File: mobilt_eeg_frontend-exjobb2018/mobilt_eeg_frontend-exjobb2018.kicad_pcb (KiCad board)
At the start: 2 copper layers, 91 x 90.4 mm, 125 parts, among them J1 Conn_02x04_Odd_Even, J11 Conn_01x02, J2 Conn_02x20_Odd_Even, J3 Conn_02x04_Odd_Even, J5 Data Header, J8 Conn_01x08, J9 Conn_01x04, P1 Conn_02x20_Odd_Even, SW1 SW_DIP_x01, SW2 SW_DIP_x01, U1 ADS1299-4PAG, U2 TPS60403DBVR, U3 TPS72325DBVT, U4 TPS73225DBVT, U5 TPS73233DBVT, U6 CAT24C256, X1 X1G0044810050_SG7050CAN_2.048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

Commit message: eagle import experiments
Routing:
- net AVDD: track 76.9 -> 69.5 mm
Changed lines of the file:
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@@
     (thickness 1.6)
     (drawings 156)
-    (tracks 990)
+    (tracks 985)
     (zones 0)
     (modules 125)
@@
     (pad_to_mask_clearance 0)
     (aux_axis_origin 200 150)
-    (grid_origin 208.37 96.23)
     (visible_elements 7FFFFFFF)
     (pcbplotparams
@@
     (add_net GNDD)
   )
+  (module LEDs:LED_D3.0mm (layer F.Cu)
+    (at 259.5 124.5)
+    (descr "LED, diameter 3.0mm, 2 pins")
+    (tags "LED diameter 3.0mm 2 pins")
+    (fp_text reference D1 (at 4.5 0 90) (layer F.SilkS)
+      (effects (font (size 1 1) (thickness 0.15)))
+    )
+    (fp_text value LED (at 1.27 2.96) (layer F.Fab)
+      (effects (font (size 1 1) (thickness 0.15)))
+    )
+    (fp_line (start 3.7 -2.25) (end -1.15 -2.25) (layer F.CrtYd) (width 0.05))
+    (fp_line (start 3.7 2.25) (end 3.7 -2.25) (layer F.CrtYd) (width 0.05))
+    (fp_line (start -1.15 2.25) (end 3.7 2.25) (layer F.CrtYd) (width 0.05))
+    (fp_line (start -1.15 -2.25) (end -1.15 2.25) (layer F.CrtYd) (width 0.05))
+    (fp_line (start -0.29 1.08) (end -0.29 1.236) (layer F.SilkS) (width 0.12))
+    (fp_line (start -0.29 -1.236) (end -0.29 -1.08) (layer F.SilkS) (width 0.12))
+    (fp_line (start -0.23 -1.16619) (end -0.23 1.16619) (layer F.Fab) (width 0.1))
+    (fp_circle (center 1.27 0) (end 2.77 0) (layer F.Fab) (width 0.1))
+    (fp_arc (start 1.27 0) (end 0.229039 1.08) (angle -87.9) (layer F.SilkS) (width 0.12))
+    (fp_arc (start 1.27 0) (end 0.229039 -1.08) (angle 87.9) (layer F.SilkS) (width 0.12))
+    (fp_arc (start 1.27 0) (end -0.29 1.235516) (angle -108.8) (layer F.SilkS) (width 0.12))
+    (fp_arc (start 1.27 0) (end -0.29 -1.235516) (angle 108.8) (layer F.SilkS) (width 0.12))
+    (fp_arc (start 1.27 0) (end -0.23 -1.16619) (angle 284.3) (layer F.Fab) (width 0.1))
+    (pad 2 thru_hole circle (at 2.54 0) (size 1.8 1.8) (drill 0.9) (layers *.Cu *.Mask)
+      (net 78 "Net-(D1-Pad2)"))
+    (pad 1 thru_hole rect (at 0 0) (size 1.8 1.8) (drill 0.9) (layers *.Cu *.Mask)
+      (net 43 AGND))
+    (model ${KISYS3DMOD}/LEDs.3dshapes/LED_D3.0mm.wrl
+      (at (xyz 0 0 0))
+      (scale (xyz 0.393701 0.393701 0.393701))
+      (rotate (xyz 0 0 0))
+    )
+  )
   (module prj_lib_fp:CP_Tantalum_Case-D_EIA-7343-31_Hand (layer F.Cu)
     (at 249.885 125.61)
@@
   )
   (module LEDs:LED_D3.0mm (layer F.Cu)
-    (at 259.5 124.5)
-    (descr "LED, diameter 3.0mm, 2 pins")
-    (tags "LED diameter 3.0mm 2 pins")
-    (fp_text reference D1 (at 4.5 0 90) (layer F.SilkS)
-      (effects (font (size 1 1) (thickness 0.15)))
-    )
-    (fp_text value LED (at 1.27 2.96) (layer F.Fab)
-      (effects (font (size 1 1) (thickness 0.15)))
-    )
-    (fp_line (start 3.7 -2.25) (end -1.15 -2.25) (layer F.CrtYd) (width 0.05))
-    (fp_line (start 3.7 2.25) (end 3.7 -2.25) (layer F.CrtYd) (width 0.05))
-    (fp_line (start -1.15 2.25) (end 3.7 2.25) (layer F.CrtYd) (width 0.05))
-    (fp_line (start -1.15 -2.25) (end -1.15 2.25) (layer F.CrtYd) (width 0.05))
-    (fp_line (start -0.29 1.08) (end -0.29 1.236) (layer F.SilkS) (width 0.12))
-    (fp_line (start -0.29 -1.236) (end -0.29 -1.08) (layer F.SilkS) (width 0.12))
-    (fp_line (start -0.23 -1.16619) (end -0.23 1.16619) (layer F.Fab) (width 0.1))
-    (fp_circle (center 1.27 0) (end 2.77 0) (layer F.Fab) (width 0.1))
-    (fp_arc (start 1.27 0) (end 0.229039 1.08) (angle -87.9) (layer F.SilkS) (width 0.12))
-    (fp_arc (start 1.27 0) (end 0.229039 -1.08) (angle 87.9) (layer F.SilkS) (width 0.12))
-    (fp_arc (start 1.27 0) (end -0.29 1.235516) (angle -108.8) (layer F.SilkS) (width 0.12))
-    (fp_arc (start 1.27 0) (end -0.29 -1.235516) (angle 108.8) (layer F.SilkS) (width 0.12))
-    (fp_arc (start 1.27 0) (end -0.23 -1.16619) (angle 284.3) (layer F.Fab) (width 0.1))
-    (pad 2 thru_hole circle (at 2.54 0) (size 1.8 1.8) (drill 0.9) (layers *.Cu *.Mask)
-      (net 78 "Net-(D1-Pad2)"))
-    (pad 1 thru_hole rect (at 0 0) (size 1.8 1.8) (drill 0.9) (layers *.Cu *.Mask)
-      (net 43 AGND))
-    (model ${KISYS3DMOD}/LEDs.3dshapes/LED_D3.0mm.wrl
-      (at (xyz 0 0 0))
-      (scale (xyz 0.393701 0.393701 0.393701))
-      (rotate (xyz 0 0 0))
-    )
-  )
-  (module LEDs:LED_D3.0mm (layer F.Cu)
     (at 259.5 115.5)
     (descr "LED, diameter 3.0mm, 2 pins")
@@
     (effects (font (size 1 1) (thickness 0.15)))
   )
-  (gr_text CAMERA (at 248 138.5 90) (layer F.SilkS)
+  (gr_text CAMERA (at 247.613 138.5 90) (layer F.SilkS)
     (effects (font (size 1 1) (thickness 0.2)))
   )
@@
   (segment (start 236.36 132.8) (end 230.45 132.8) (width 0.25) (layer F.Cu) (net 70) (status 30))
   (segment (start 230.25 130) (end 230.25 133) (width 0.25) (layer F.Cu) (net 70) (status 30))
-  (segment (start 186.9692 129.7954) (end 188 128.7646) (width 0.25) (layer F.Cu) (net 70))
-  (segment (start 186.4398 129.7954) (end 186.9692 129.7954) (width 0.25) (layer F.Cu) (net 70) (status 10))
-  (segment (start 189.75 124.875) (end 189.75 124) (width 0.25) (layer F.Cu) (net 70) (status 20))
-  (segment (start 188 126.625) (end 189.75 124.875) (width 0.25) (layer F.Cu) (net 70))
-  (segment (start 188 128.7646) (end 188 126.625) (width 0.25) (layer F.Cu) (net 70))
   (segment (start 230.25 136) (end 230.25 135.125) (width 0.25) (layer F.Cu) (net 70) (status 10))
   (segment (start 238.9 135.34) (end 238.9 134.137919) (width 0.25) (layer F.Cu) (net 70) (status 10))

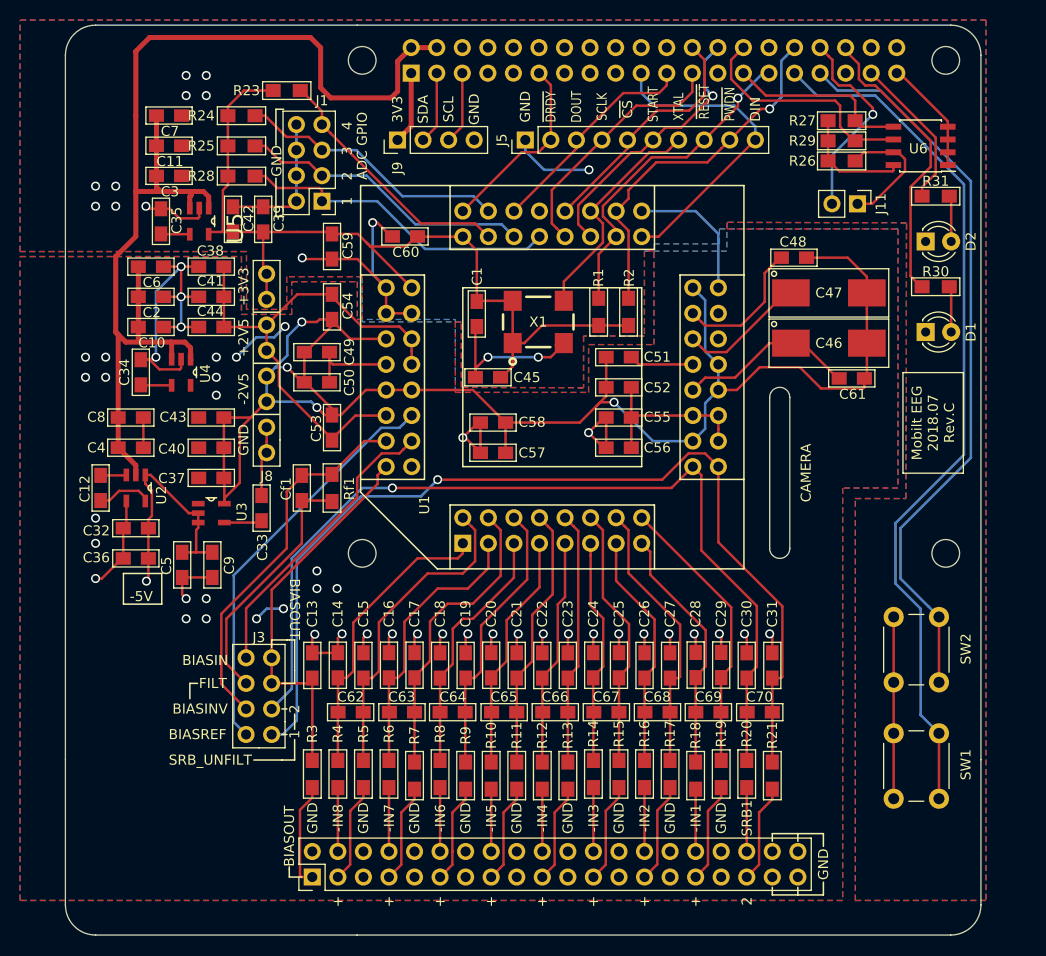
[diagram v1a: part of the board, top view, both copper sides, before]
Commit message: adjusted bias header to conform to 2.54 grid
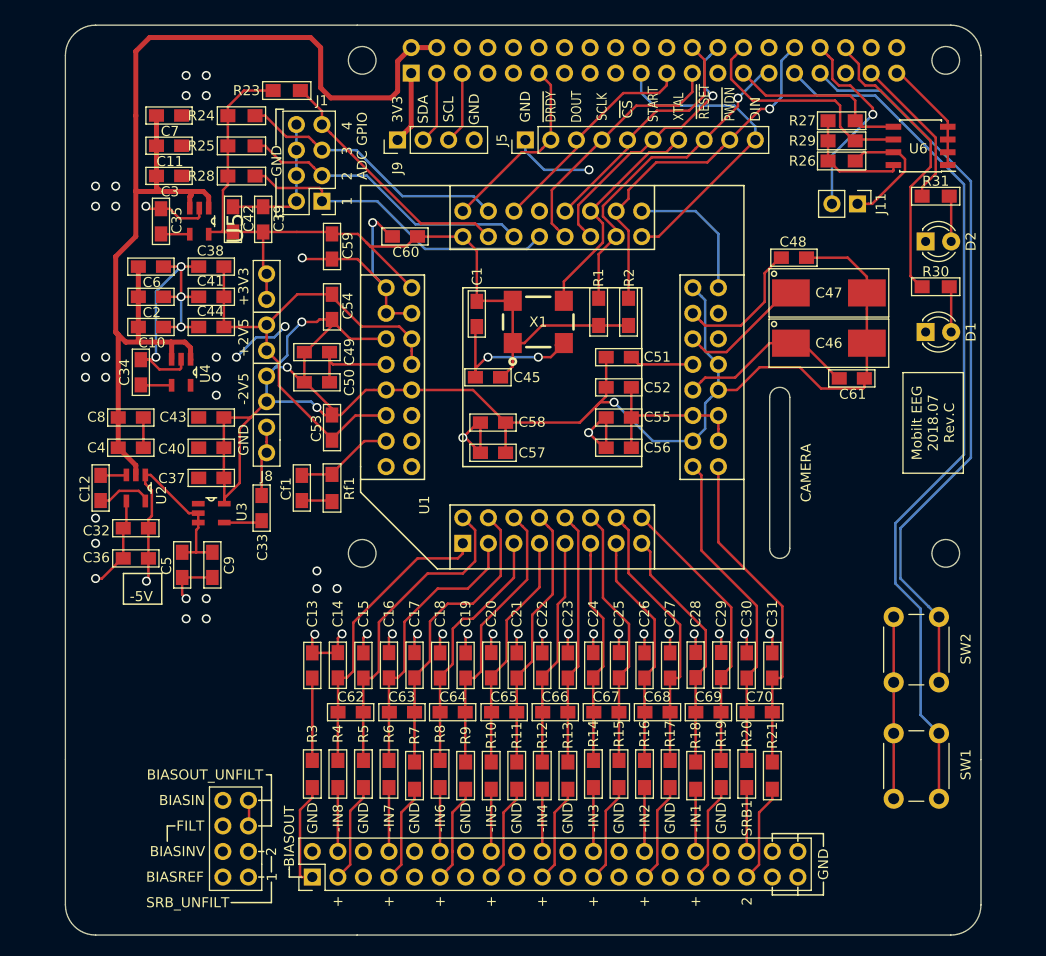
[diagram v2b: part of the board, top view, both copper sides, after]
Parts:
- moved J3 14.4 mm to (192.2, 178.7)
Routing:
- net /SRB1: track 98.7 -> 32.9 mm, vias 1 -> 0
- net /SRB2: track 91.7 -> 32.3 mm, vias 1 -> 0
- net /BIASREF: track 40.6 -> 0.00 mm
- net /BIASIN: track 29.4 -> 0.00 mm
- net /BIASOUT: track 38.7 -> 10.7 mm
- net /BIASINV: track 37.4 -> 9.85 mm
- net Net-(Cf1-Pad2): track 25.1 -> 3.04 mm
- net AGND: track 255.4 -> 252.3 mm, vias 61 -> 59
- removed copper zone on B.Cu, net AGND
- removed copper zone on F.Cu, net AGND
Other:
- board text added: "BIASOUT_UNFILT"

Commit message: before nightly update
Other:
- board text added: "2.54mm grid origin - Pi header pin 1 1mm grid origin"
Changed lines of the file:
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@@
   (general
     (thickness 1.6)
-    (drawings 150)
+    (drawings 151)
     (tracks 933)
     (zones 0)
@@
     (pad_to_mask_clearance 0)
     (aux_axis_origin 200 150)
-    (grid_origin 198.54 178.67)
     (visible_elements 7FFFFFFF)
     (pcbplotparams
@@
       (net 1 +5V))
   )
+  (gr_text "2.54mm grid origin - Pi header pin 1\n1mm grid origin" (at 212.344 83.058) (layer Eco2.User)
+    (effects (font (size 1 1) (thickness 0.25)))
+  )
   (gr_line (start 194.476 168.51) (end 193.968 168.51) (layer F.SilkS) (width 0.15))

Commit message: MADE IN SWEDEN
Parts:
- moved J5 1.53 mm to (218.5, 106.4)
- moved J9 1.53 mm to (205.8, 106.4)
- moved U1 0.26 mm to (213.4, 145.8)
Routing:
- net /GPIO10(SPI0_MOSI): track 31.3 -> 14.8 mm
- net /~RESET: track 32.9 -> 19.9 mm
- net /XTAL: track 22.7 -> 11.0 mm
- net /~PWDN: track 36.3 -> 24.7 mm
- net /~DRDY: track 18.8 -> 7.62 mm
- net /START: track 27.2 -> 16.6 mm
- net /GPIO11(SPI0_SCK): track 25.0 -> 17.0 mm
- net /+3V3_Pi: track 7.20 -> 0.00 mm
- net /GPIO3(SCL1): track 7.20 -> 0.00 mm
- net /GPIO2(SDA1): track 7.20 -> 0.00 mm
- net /GPIO8(SPI0_CE_N): track 24.4 -> 18.5 mm
- net /GPIO9(SPI0_MISO): track 22.1 -> 16.3 mm
- net AGND: track 252.3 -> 251.7 mm, vias 59 -> 55
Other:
- board text added: "GRID OVERHAUL"
- board text added: "MADE IN SWEDEN"
- board text added: "Notes All 2.54mm headers conform to 2.54mm grid with origo on Pi header pin 1. All SMD components conform to 1mm grid with origo on Pi header pin 1."
- board text removed: "2.54mm grid origin - Pi header pin 1 1mm grid origin"
- board text removed: "ALT PCB 1"

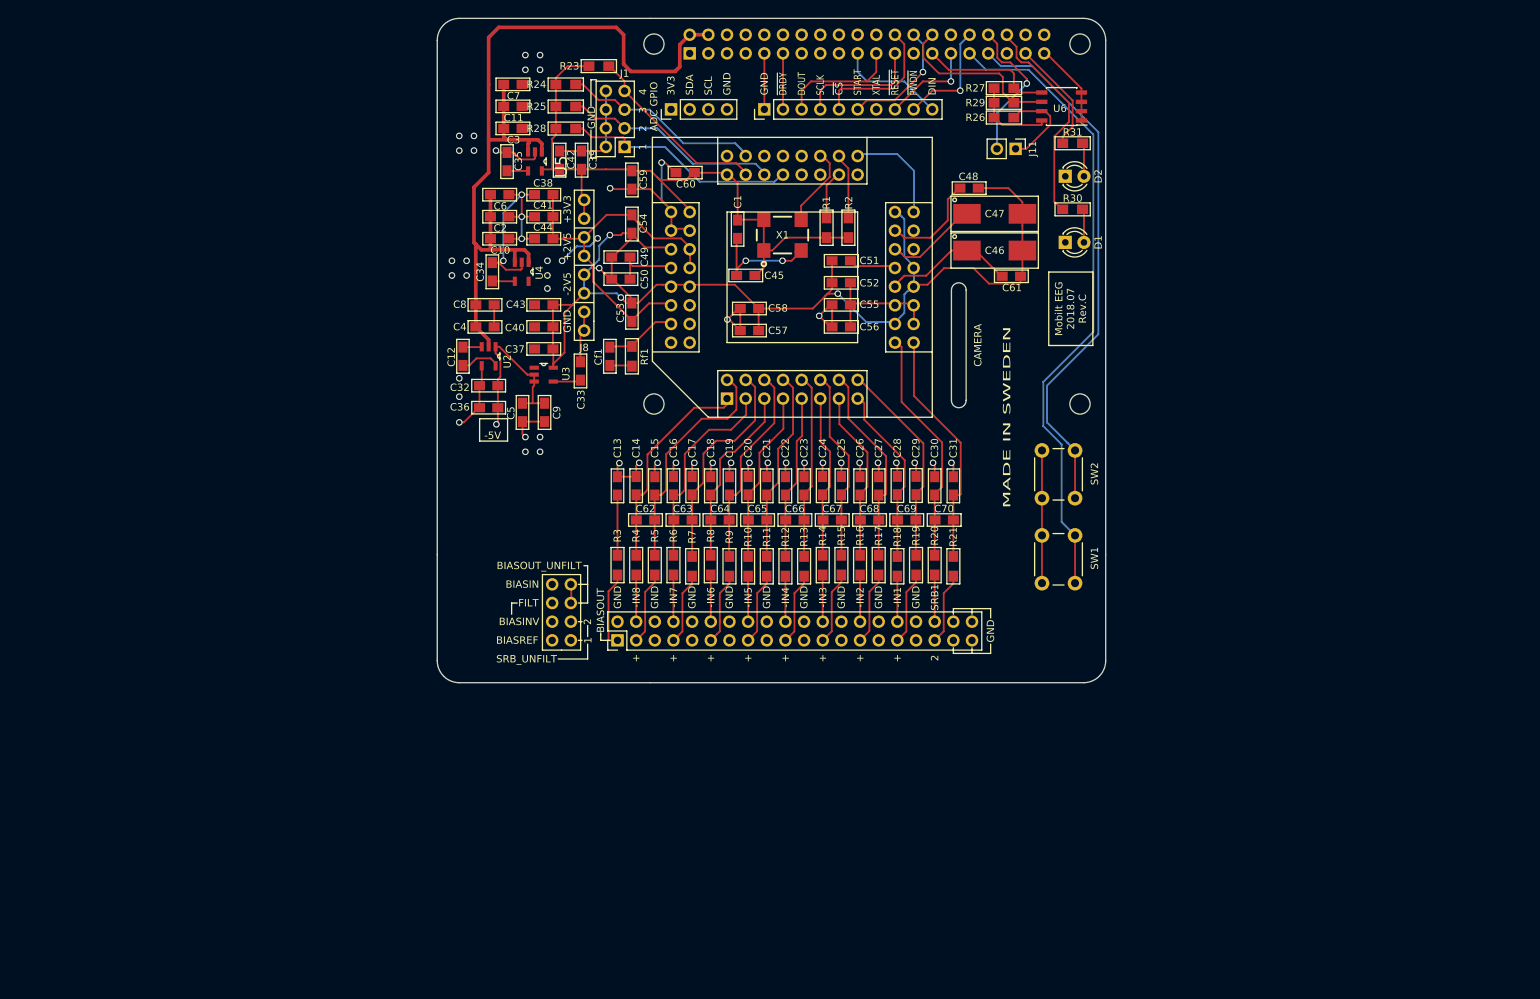
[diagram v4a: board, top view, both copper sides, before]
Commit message: Gave caps and resistors custom footprint assignment. created arduino pro mini 3v3 sparkfun module in schema and pcb footprint. Deleted extraneous vias.
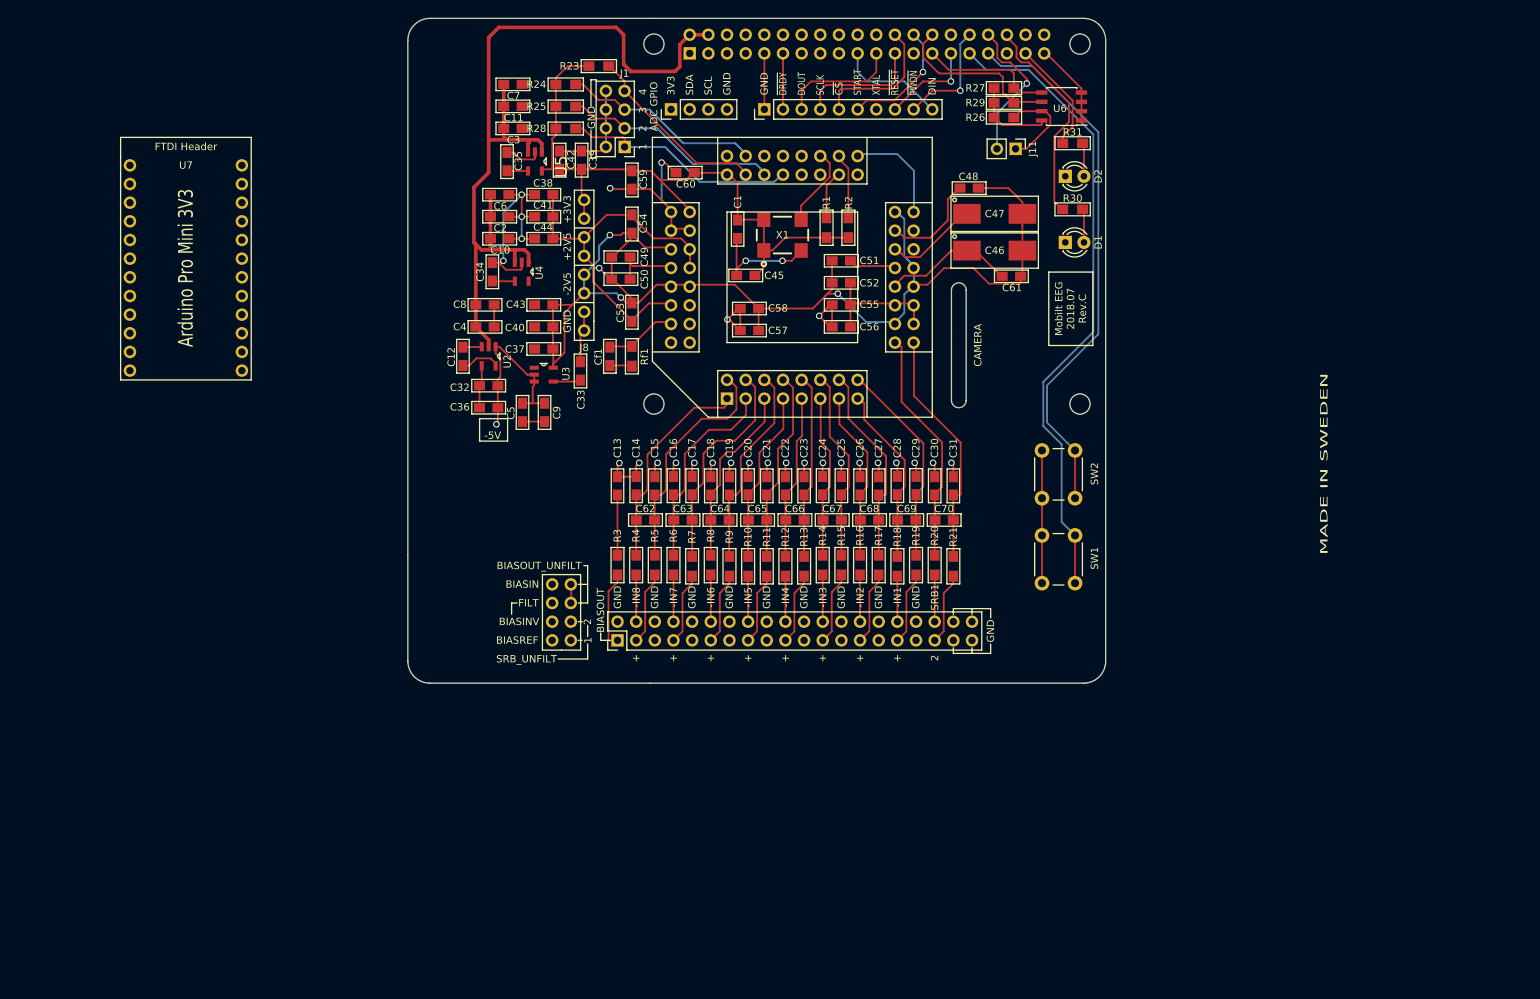
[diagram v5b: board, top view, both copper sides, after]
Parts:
- added U7: arduino_pro_mini_3V3_sparkfun, prj_lib_fp:arduino_pro_mini_3V3_sparkfun, F.Cu at (132.2, 114.0)
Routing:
- net AGND: track 251.7 -> 238.2 mm, vias 55 -> 30
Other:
- board size 91 x 90.4 mm -> 95 x 90.5 mm
